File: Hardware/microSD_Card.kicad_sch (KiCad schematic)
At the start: 1 part

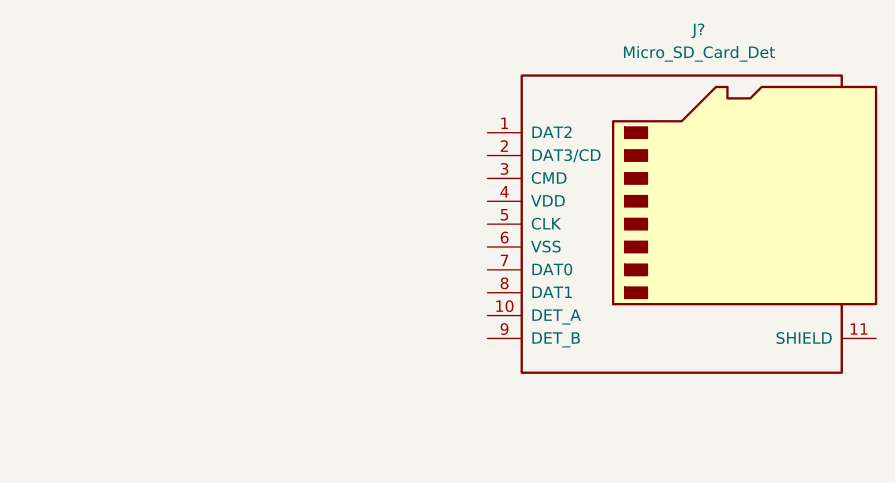
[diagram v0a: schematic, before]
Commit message: added msd slot
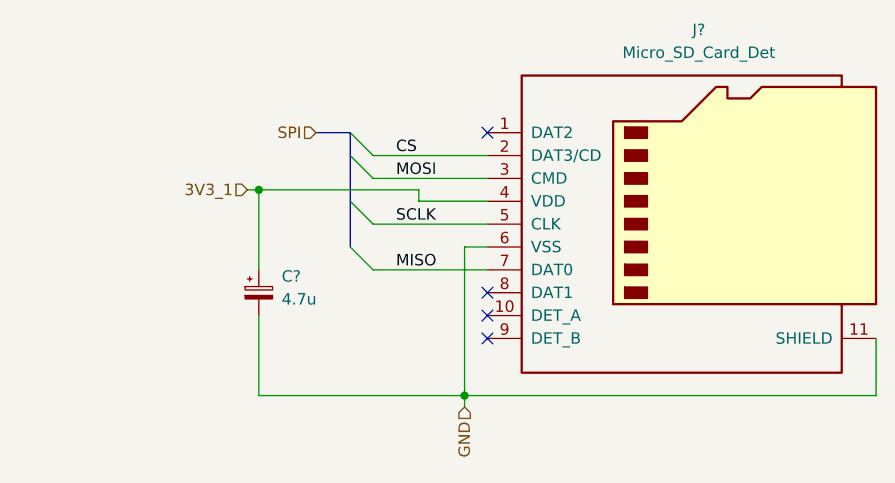
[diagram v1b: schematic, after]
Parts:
- added C?: 4.7u, symbol Device:C_Polarized_Small
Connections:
- net GND: now reaches J?.11 (SHIELD)
- net GND: now also J?.6 (VSS), C?.2
- net CS: now reaches J?.2 (DAT3/CD)
- net MOSI: now reaches J?.3 (CMD)
- net 3V3_1: now reaches J?.4 (VDD)
- net 3V3_1: now also C?.1
- net SCLK: now reaches J?.5 (CLK)
- net MISO: now reaches J?.7 (DAT0)
- no-connect marks 0 -> 4
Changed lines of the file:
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@@
 (kicad_sch (version 20211123) (generator eeschema)
   (paper "A4")
+  (junction (at 121.92 107.95) (diameter 0) (color 0 0 0 0)
+  )
+  (junction (at 99.06 85.09) (diameter 0) (color 0 0 0 0)
+  )
+  (no_connect (at 124.46 78.74))
+  (no_connect (at 124.46 101.6))
+  (no_connect (at 124.46 99.06))
+  (no_connect (at 124.46 96.52))
+  (bus_entry (at 109.22 91.44) (size 2.54 2.54)
+    (stroke (width 0) (type default) (color 0 0 0 0))
+  )
+  (bus_entry (at 109.22 81.28) (size 2.54 2.54)
+    (stroke (width 0) (type default) (color 0 0 0 0))
+  )
+  (bus_entry (at 109.22 78.74) (size 2.54 2.54)
+    (stroke (width 0) (type default) (color 0 0 0 0))
+  )
+  (bus_entry (at 109.22 86.36) (size 2.54 2.54)
+    (stroke (width 0) (type default) (color 0 0 0 0))
+  )
+  (wire (pts (xy 111.76 93.98) (xy 124.46 93.98))
+    (stroke (width 0) (type default) (color 0 0 0 0))
+  )
+  (bus (pts (xy 105.41 78.74) (xy 109.22 78.74))
+    (stroke (width 0) (type default) (color 0 0 0 0))
+  )
+  (wire (pts (xy 111.76 88.9) (xy 124.46 88.9))
+    (stroke (width 0) (type default) (color 0 0 0 0))
+  )
+  (wire (pts (xy 111.76 81.28) (xy 124.46 81.28))
+    (stroke (width 0) (type default) (color 0 0 0 0))
+  )
+  (wire (pts (xy 121.92 107.95) (xy 167.64 107.95))
+    (stroke (width 0) (type default) (color 0 0 0 0))
+  )
+  (wire (pts (xy 99.06 85.09) (xy 116.84 85.09))
+    (stroke (width 0) (type default) (color 0 0 0 0))
+  )
+  (wire (pts (xy 167.64 101.6) (xy 167.64 107.95))
+    (stroke (width 0) (type default) (color 0 0 0 0))
+  )
+  (wire (pts (xy 121.92 107.95) (xy 121.92 109.22))
+    (stroke (width 0) (type default) (color 0 0 0 0))
+  )
+  (wire (pts (xy 121.92 91.44) (xy 121.92 107.95))
+    (stroke (width 0) (type default) (color 0 0 0 0))
+  )
+  (wire (pts (xy 99.06 107.95) (xy 121.92 107.95))
+    (stroke (width 0) (type default) (color 0 0 0 0))
+  )
+  (wire (pts (xy 111.76 83.82) (xy 124.46 83.82))
+    (stroke (width 0) (type default) (color 0 0 0 0))
+  )
+  (wire (pts (xy 121.92 91.44) (xy 124.46 91.44))
+    (stroke (width 0) (type default) (color 0 0 0 0))
+  )
+  (bus (pts (xy 109.22 81.28) (xy 109.22 86.36))
+    (stroke (width 0) (type default) (color 0 0 0 0))
+  )
+  (wire (pts (xy 116.84 86.36) (xy 116.84 85.09))
+    (stroke (width 0) (type default) (color 0 0 0 0))
+  )
+  (wire (pts (xy 97.79 85.09) (xy 99.06 85.09))
+    (stroke (width 0) (type default) (color 0 0 0 0))
+  )
+  (bus (pts (xy 109.22 86.36) (xy 109.22 91.44))
+    (stroke (width 0) (type default) (color 0 0 0 0))
+  )
+  (wire (pts (xy 99.06 85.09) (xy 99.06 93.98))
+    (stroke (width 0) (type default) (color 0 0 0 0))
+  )
+  (bus (pts (xy 109.22 78.74) (xy 109.22 81.28))
+    (stroke (width 0) (type default) (color 0 0 0 0))
+  )
+  (wire (pts (xy 99.06 99.06) (xy 99.06 107.95))
+    (stroke (width 0) (type default) (color 0 0 0 0))
+  )
+  (wire (pts (xy 124.46 86.36) (xy 116.84 86.36))
+    (stroke (width 0) (type default) (color 0 0 0 0))
+  )
+  (label "CS" (at 114.3 81.28 0)
+    (effects (font (size 1.27 1.27)) (justify left bottom))
+  )
+  (label "SCLK" (at 114.3 88.9 0)
+    (effects (font (size 1.27 1.27)) (justify left bottom))
+  )
+  (label "MISO" (at 114.3 93.98 0)
+    (effects (font (size 1.27 1.27)) (justify left bottom))
+  )
+  (label "MOSI" (at 114.3 83.82 0)
+    (effects (font (size 1.27 1.27)) (justify left bottom))
+  )
+  (hierarchical_label "SPI" (shape input) (at 105.41 78.74 180)
+    (effects (font (size 1.27 1.27)) (justify right))
+  )
+  (hierarchical_label "3V3_1" (shape input) (at 97.79 85.09 180)
+    (effects (font (size 1.27 1.27)) (justify right))
+  )
+  (hierarchical_label "GND" (shape input) (at 121.92 109.22 270)
+    (effects (font (size 1.27 1.27)) (justify right))
+  )
   (symbol (lib_id "Connector:Micro_SD_Card_Det") (at 147.32 88.9 0) (unit 1)
     (in_bom yes) (on_board yes) (fields_autoplaced)
@@
     (pin "9")
   )
+  (symbol (lib_id "Device:C_Polarized_Small") (at 99.06 96.52 0) (unit 1)
+    (in_bom yes) (on_board yes) (fields_autoplaced)
+    (property "Reference" "C?" (id 0) (at 101.6 94.7038 0)
+      (effects (font (size 1.27 1.27)) (justify left))
+    )
+    (property "Value" "4.7u" (id 1) (at 101.6 97.2438 0)
+      (effects (font (size 1.27 1.27)) (justify left))
+    )
+    (property "Footprint" "" (id 2) (at 99.06 96.52 0)
+      (effects (font (size 1.27 1.27)) hide)
+    )
+    (property "Datasheet" "~" (id 3) (at 99.06 96.52 0)
+      (effects (font (size 1.27 1.27)) hide)
+    )
+    (pin "1")
+    (pin "2")
+  )
 )

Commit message: included psu on pcb
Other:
- company: (none) -> ncAudio
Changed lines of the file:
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@@
 (kicad_sch (version 20211123) (generator eeschema)
   (paper "A4")
+  (title_block
+    (date "2022-12-27")
+    (rev "0.1")
+    (company "ncAudio")
+  )
   (junction (at 121.92 107.95) (diameter 0) (color 0 0 0 0)
   )

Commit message: cleaned up busses
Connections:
- net 3V3_1 renamed 3V3
- net CS renamed SPI.~{CS}
- net MISO renamed SPI.MISO
- net MOSI renamed SPI.MOSI
- net SCLK renamed SPI.SCK
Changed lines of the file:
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@@
     (company "ncAudio")
   )
+  (junction (at 99.06 85.09) (diameter 0) (color 0 0 0 0)
+  )
   (junction (at 121.92 107.95) (diameter 0) (color 0 0 0 0)
-  )
-  (junction (at 99.06 85.09) (diameter 0) (color 0 0 0 0)
   )
   (no_connect (at 124.46 78.74))
@@
   (no_connect (at 124.46 99.06))
   (no_connect (at 124.46 96.52))
-  (bus_entry (at 109.22 91.44) (size 2.54 2.54)
+  (bus_entry (at 109.22 81.28) (size 2.54 2.54)
     (stroke (width 0) (type default) (color 0 0 0 0))
   )
-  (bus_entry (at 109.22 81.28) (size 2.54 2.54)
+  (bus_entry (at 109.22 86.36) (size 2.54 2.54)
     (stroke (width 0) (type default) (color 0 0 0 0))
   )
@@
     (stroke (width 0) (type default) (color 0 0 0 0))
   )
-  (bus_entry (at 109.22 86.36) (size 2.54 2.54)
+  (bus_entry (at 109.22 91.44) (size 2.54 2.54)
     (stroke (width 0) (type default) (color 0 0 0 0))
   )
-  (wire (pts (xy 111.76 93.98) (xy 124.46 93.98))
+  (wire (pts (xy 111.76 83.82) (xy 124.46 83.82))
     (stroke (width 0) (type default) (color 0 0 0 0))
   )
-  (bus (pts (xy 105.41 78.74) (xy 109.22 78.74))
-    (stroke (width 0) (type default) (color 0 0 0 0))
-  )
-  (wire (pts (xy 111.76 88.9) (xy 124.46 88.9))
-    (stroke (width 0) (type default) (color 0 0 0 0))
-  )
-  (wire (pts (xy 111.76 81.28) (xy 124.46 81.28))
+  (bus (pts (xy 109.22 81.28) (xy 109.22 86.36))
     (stroke (width 0) (type default) (color 0 0 0 0))
   )
@@
     (stroke (width 0) (type default) (color 0 0 0 0))
   )
-  (wire (pts (xy 99.06 85.09) (xy 116.84 85.09))
+  (wire (pts (xy 124.46 86.36) (xy 124.46 85.09))
+    (stroke (width 0) (type default) (color 0 0 0 0))
+  )
+  (wire (pts (xy 124.46 85.09) (xy 99.06 85.09))
     (stroke (width 0) (type default) (color 0 0 0 0))
   )
   (wire (pts (xy 167.64 101.6) (xy 167.64 107.95))
+    (stroke (width 0) (type default) (color 0 0 0 0))
+  )
+  (wire (pts (xy 111.76 81.28) (xy 124.46 81.28))
     (stroke (width 0) (type default) (color 0 0 0 0))
   )
@@
     (stroke (width 0) (type default) (color 0 0 0 0))
   )
-  (wire (pts (xy 99.06 107.95) (xy 121.92 107.95))
+  (wire (pts (xy 99.06 85.09) (xy 99.06 93.98))
     (stroke (width 0) (type default) (color 0 0 0 0))
   )
-  (wire (pts (xy 111.76 83.82) (xy 124.46 83.82))
+  (wire (pts (xy 99.06 107.95) (xy 121.92 107.95))
     (stroke (width 0) (type default) (color 0 0 0 0))
   )
@@
     (stroke (width 0) (type default) (color 0 0 0 0))
   )
-  (bus (pts (xy 109.22 81.28) (xy 109.22 86.36))
+  (bus (pts (xy 109.22 78.74) (xy 109.22 81.28))
     (stroke (width 0) (type default) (color 0 0 0 0))
   )
-  (wire (pts (xy 116.84 86.36) (xy 116.84 85.09))
+  (wire (pts (xy 111.76 93.98) (xy 124.46 93.98))
     (stroke (width 0) (type default) (color 0 0 0 0))
   )
@@
     (stroke (width 0) (type default) (color 0 0 0 0))
   )
-  (wire (pts (xy 99.06 85.09) (xy 99.06 93.98))
-    (stroke (width 0) (type default) (color 0 0 0 0))
-  )
-  (bus (pts (xy 109.22 78.74) (xy 109.22 81.28))
+  (bus (pts (xy 105.41 78.74) (xy 109.22 78.74))
     (stroke (width 0) (type default) (color 0 0 0 0))
   )
@@
     (stroke (width 0) (type default) (color 0 0 0 0))
   )
-  (wire (pts (xy 124.46 86.36) (xy 116.84 86.36))
+  (wire (pts (xy 111.76 88.9) (xy 124.46 88.9))
     (stroke (width 0) (type default) (color 0 0 0 0))
   )
-  (label "CS" (at 114.3 81.28 0)
+  (label "SPI.SCK" (at 113.03 88.9 0)
     (effects (font (size 1.27 1.27)) (justify left bottom))
   )
-  (label "SCLK" (at 114.3 88.9 0)
+  (label "SPI.~{CS}" (at 113.03 81.28 0)
     (effects (font (size 1.27 1.27)) (justify left bottom))
   )
-  (label "MISO" (at 114.3 93.98 0)
+  (label "SPI.MISO" (at 113.03 93.98 0)
     (effects (font (size 1.27 1.27)) (justify left bottom))
   )
-  (label "MOSI" (at 114.3 83.82 0)
+  (label "SPI.MOSI" (at 113.03 83.82 0)
     (effects (font (size 1.27 1.27)) (justify left bottom))
   )
-  (hierarchical_label "SPI" (shape input) (at 105.41 78.74 180)
+  (hierarchical_label "SPI{MOSI MISO SCK ~{CS}}" (shape input) (at 105.41 78.74 180)
     (effects (font (size 1.27 1.27)) (justify right))
   )
-  (hierarchical_label "3V3_1" (shape input) (at 97.79 85.09 180)
-    (effects (font (size 1.27 1.27)) (justify right))
-  )
-  (hierarchical_label "GND" (shape input) (at 121.92 109.22 270)
+  (hierarchical_label "3V3" (shape input) (at 97.79 85.09 180)
     (effects (font (size 1.27 1.27)) (justify right))
   )
@@
     (pin "9")
   )
+  (symbol (lib_id "power:GND") (at 121.92 109.22 0) (unit 1)
+    (in_bom yes) (on_board yes) (fields_autoplaced)
+    (property "Reference" "#PWR?" (id 0) (at 121.92 115.57 0)
+      (effects (font (size 1.27 1.27)) hide)
+    )
+    (property "Value" "GND" (id 1) (at 121.92 114.3 0))
+    (property "Footprint" "" (id 2) (at 121.92 109.22 0)
+      (effects (font (size 1.27 1.27)) hide)
+    )
+    (property "Datasheet" "" (id 3) (at 121.92 109.22 0)
+      (effects (font (size 1.27 1.27)) hide)
+    )
+    (pin "1")
+  )
   (symbol (lib_id "Device:C_Polarized_Small") (at 99.06 96.52 0) (unit 1)
